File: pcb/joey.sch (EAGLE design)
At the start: 61 parts, among them J1 AVR_SPI_PRG_6PTH, U1 ATMEGA168, U2 TMP102, X1 USB-MICROB, Y1 13.56M

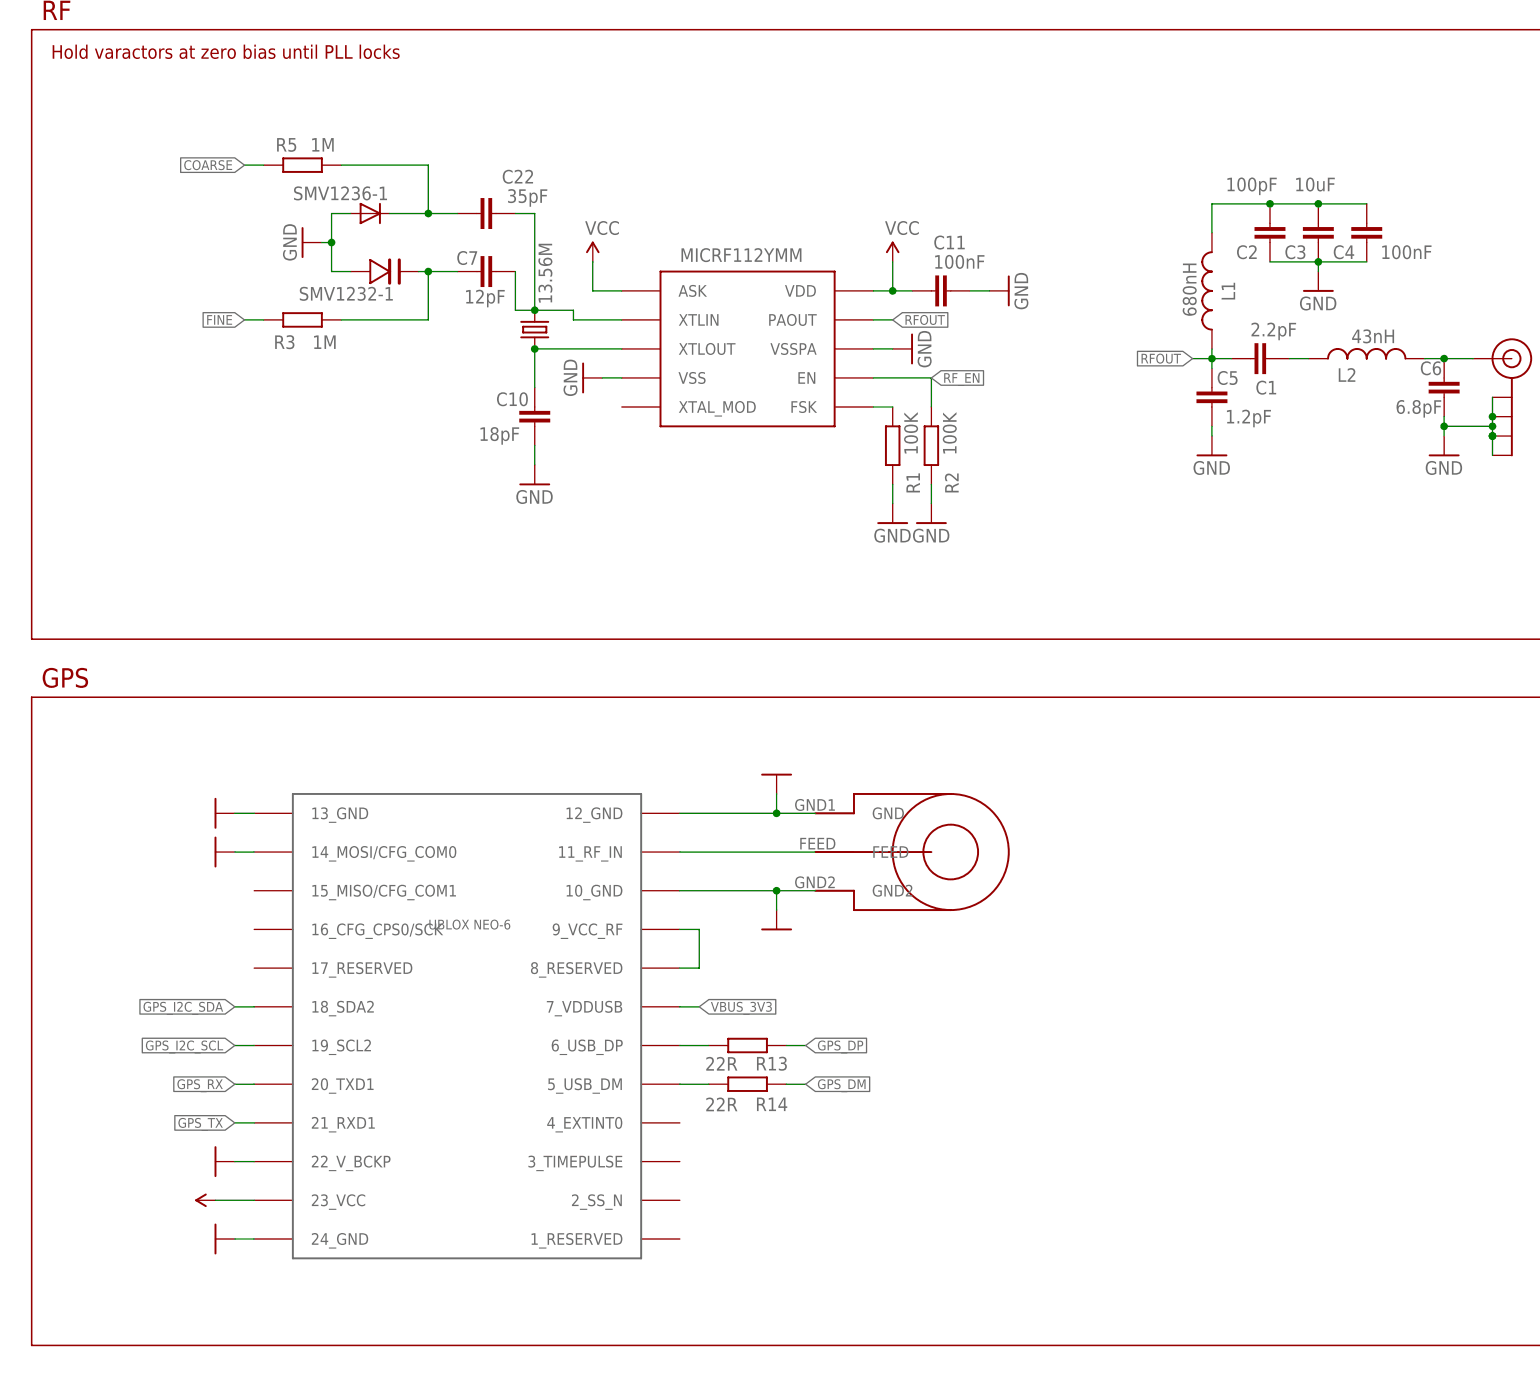
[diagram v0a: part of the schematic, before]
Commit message: Fixed filter bug in the schematic, almost finished routing
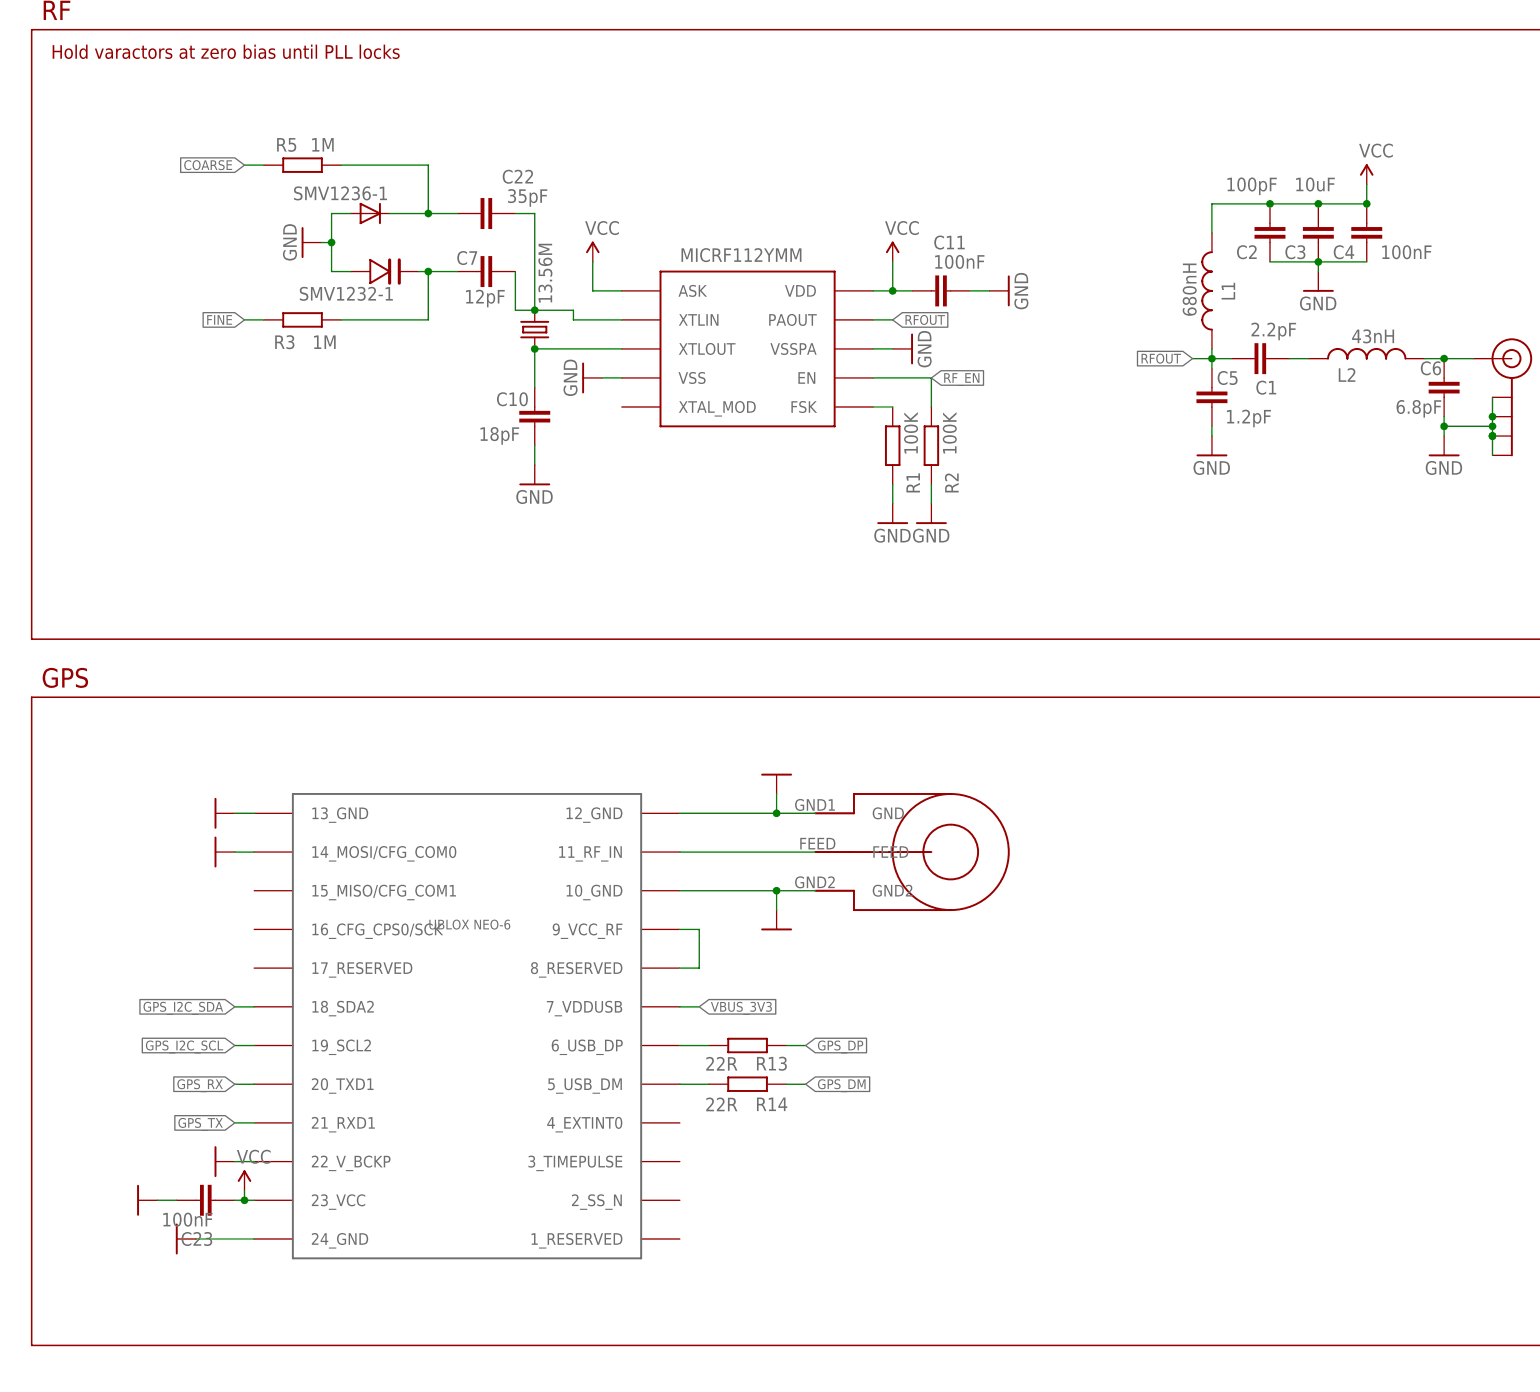
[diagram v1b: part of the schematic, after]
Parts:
- added C23: 100nF, rcl:C-EUC0603
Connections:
- removed net N$4: C2.2, C3.2, C4.2, L1.2
- new net COARSE_V: C22.1, R5.2, SMV1236-1.C
- net COARSE: no longer C22.1, R5.2, SMV1236-1.C
- net GND: now also C23.1
- net VCC: now also C2.2, C23.2, C3.2, C4.2, L1.2
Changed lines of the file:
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@@
 <part name="GND17" library="SparkFun" deviceset="GND" device=""/>
 <part name="GND18" library="SparkFun" deviceset="GND" device=""/>
-<part name="P+3" library="SparkFun" deviceset="VCC" device=""/>
 <part name="GND19" library="SparkFun" deviceset="GND" device=""/>
 <part name="GND20" library="SparkFun" deviceset="GND" device=""/>
@@
 <part name="GND34" library="SparkFun" deviceset="GND" device=""/>
 <part name="P+6" library="SparkFun" deviceset="VCC" device=""/>
+<part name="C23" library="rcl" deviceset="C-EU" device="C0603" value="100nF"/>
+<part name="GND35" library="SparkFun" deviceset="GND" device=""/>
+<part name="P+3" library="SparkFun" deviceset="VCC" device=""/>
+<part name="P+13" library="SparkFun" deviceset="VCC" device=""/>
 </parts>
 <sheets>
@@
 <instance part="U$2" gate="G$1" x="142.24" y="-62.23" smashed="yes" rot="R180"/>
 <instance part="U$3" gate="G$1" x="83.82" y="-67.31"/>
-<instance part="GND16" gate="1" x="48.26" y="-115.57" smashed="yes" rot="R270"/>
+<instance part="GND16" gate="1" x="43.18" y="-115.57" smashed="yes" rot="R270"/>
 <instance part="GND17" gate="1" x="48.26" y="-59.69" smashed="yes" rot="R270"/>
 <instance part="GND18" gate="1" x="48.26" y="-105.41" smashed="yes" rot="R270"/>
-<instance part="P+3" gate="1" x="48.26" y="-110.49" smashed="yes" rot="R90"/>
 <instance part="GND19" gate="1" x="121.92" y="-74.93" smashed="yes"/>
 <instance part="GND20" gate="1" x="121.92" y="-54.61" smashed="yes" rot="R180"/>
@@
 <instance part="GND34" gate="1" x="-123.19" y="-66.04" rot="R270"/>
 <instance part="P+6" gate="1" x="-95.25" y="-60.96" smashed="yes"/>
+<instance part="C23" gate="G$1" x="45.72" y="-110.49" smashed="yes" rot="R90">
+<attribute name="NAME" x="48.006" y="-114.681" size="1.778" layer="95" rot="R180"/>
+<attribute name="VALUE" x="48.006" y="-112.141" size="1.778" layer="96" rot="R180"/>
+</instance>
+<instance part="GND35" gate="1" x="38.1" y="-110.49" smashed="yes" rot="R270"/>
+<instance part="P+3" gate="1" x="52.07" y="-109.22"/>
+<instance part="P+13" gate="1" x="199.39" y="22.86"/>
 </instances>
 <busses>
@@
 <pinref part="U$3" gate="G$1" pin="24_GND"/>
 <pinref part="GND16" gate="1" pin="GND"/>
-<wire x1="53.34" y1="-115.57" x2="50.8" y2="-115.57" width="0.1524" layer="91"/>
+<wire x1="53.34" y1="-115.57" x2="45.72" y2="-115.57" width="0.1524" layer="91"/>
 </segment>
 <segment>
@@
 <wire x1="-113.03" y1="-66.04" x2="-120.65" y2="-66.04" width="0.1524" layer="91"/>
 </segment>
+<segment>
+<pinref part="C23" gate="G$1" pin="1"/>
+<wire x1="43.18" y1="-110.49" x2="40.64" y2="-110.49" width="0.1524" layer="91"/>
+<pinref part="GND35" gate="1" pin="GND"/>
+</segment>
 </net>
 <net name="VCC" class="0">
@@
 <pinref part="P+4" gate="1" pin="VCC"/>
 <pinref part="J1" gate="G$1" pin="2"/>
-</segment>
-<segment>
-<pinref part="P+3" gate="1" pin="VCC"/>
-<pinref part="U$3" gate="G$1" pin="23_VCC"/>
-<wire x1="48.26" y1="-110.49" x2="53.34" y2="-110.49" width="0.1524" layer="91"/>
 </segment>
 <segment>
@@
 <pinref part="P+6" gate="1" pin="VCC"/>
 </segment>
-</net>
-<net name="N$1" class="0">
-<segment>
-<wire x1="134.62" y1="-6.35" x2="137.16" y2="-6.35" width="0.1524" layer="91"/>
-<pinref part="U$1" gate="G$1" pin="FSK"/>
-<pinref part="R1" gate="G$1" pin="2"/>
-</segment>
-</net>
-<net name="RF_EN" class="0">
-<segment>
-<wire x1="134.62" y1="-2.54" x2="142.24" y2="-2.54" width="0.1524" layer="91"/>
-<wire x1="142.24" y1="-2.54" x2="142.24" y2="-6.35" width="0.1524" layer="91"/>
-<label x="142.24" y="-2.54" size="1.27" layer="95" xref="yes"/>
-<pinref part="U$1" gate="G$1" pin="EN"/>
-<pinref part="R2" gate="G$1" pin="2"/>
-</segment>
-<segment>
-<pinref part="U1" gate="G$1" pin="PC2(ADC2)"/>
-<wire x1="-44.45" y1="-60.96" x2="-41.91" y2="-60.96" width="0.1524" layer="91"/>
-<label x="-41.91" y="-60.96" size="1.27" layer="95" xref="yes"/>
-</segment>
-</net>
-<net name="RFOUT" class="0">
-<segment>
-<wire x1="179.07" y1="-1.27" x2="179.07" y2="0" width="0.1524" layer="91"/>
-<wire x1="179.07" y1="0" x2="179.07" y2="1.27" width="0.1524" layer="91"/>
-<wire x1="179.07" y1="0" x2="181.61" y2="0" width="0.1524" layer="91"/>
-<wire x1="179.07" y1="0" x2="176.53" y2="0" width="0.1524" layer="91"/>
-<junction x="179.07" y="0"/>
-<label x="176.53" y="0" size="1.27" layer="95" rot="R180" xref="yes"/>
-<pinref part="L1" gate="G$1" pin="1"/>
-<pinref part="C5" gate="G$1" pin="2"/>
-<pinref part="C1" gate="G$1" pin="1"/>
-</segment>
-<segment>
-<wire x1="134.62" y1="5.08" x2="137.16" y2="5.08" width="0.1524" layer="91"/>
-<label x="137.16" y="5.08" size="1.27" layer="95" xref="yes"/>
-<pinref part="U$1" gate="G$1" pin="PAOUT"/>
-</segment>
-</net>
-<net name="N$4" class="0">
+<segment>
+<pinref part="C23" gate="G$1" pin="2"/>
+<pinref part="U$3" gate="G$1" pin="23_VCC"/>
+<wire x1="50.8" y1="-110.49" x2="52.07" y2="-110.49" width="0.1524" layer="91"/>
+<pinref part="P+3" gate="1" pin="VCC"/>
+<wire x1="52.07" y1="-110.49" x2="53.34" y2="-110.49" width="0.1524" layer="91"/>
+<wire x1="52.07" y1="-109.22" x2="52.07" y2="-110.49" width="0.1524" layer="91"/>
+<junction x="52.07" y="-110.49"/>
+</segment>
 <segment>
 <wire x1="179.07" y1="16.51" x2="179.07" y2="20.32" width="0.1524" layer="91"/>
@@
 <pinref part="C3" gate="G$1" pin="2"/>
 <pinref part="C4" gate="G$1" pin="2"/>
+<pinref part="P+13" gate="1" pin="VCC"/>
+<wire x1="199.39" y1="22.86" x2="199.39" y2="20.32" width="0.1524" layer="91"/>
+<junction x="199.39" y="20.32"/>
+</segment>
+</net>
+<net name="N$1" class="0">
+<segment>
+<wire x1="134.62" y1="-6.35" x2="137.16" y2="-6.35" width="0.1524" layer="91"/>
+<pinref part="U$1" gate="G$1" pin="FSK"/>
+<pinref part="R1" gate="G$1" pin="2"/>
+</segment>
+</net>
+<net name="RF_EN" class="0">
+<segment>
+<wire x1="134.62" y1="-2.54" x2="142.24" y2="-2.54" width="0.1524" layer="91"/>
+<wire x1="142.24" y1="-2.54" x2="142.24" y2="-6.35" width="0.1524" layer="91"/>
+<label x="142.24" y="-2.54" size="1.27" layer="95" xref="yes"/>
+<pinref part="U$1" gate="G$1" pin="EN"/>
+<pinref part="R2" gate="G$1" pin="2"/>
+</segment>
+<segment>
+<pinref part="U1" gate="G$1" pin="PC2(ADC2)"/>
+<wire x1="-44.45" y1="-60.96" x2="-41.91" y2="-60.96" width="0.1524" layer="91"/>
+<label x="-41.91" y="-60.96" size="1.27" layer="95" xref="yes"/>
+</segment>
+</net>
+<net name="RFOUT" class="0">
+<segment>
+<wire x1="179.07" y1="-1.27" x2="179.07" y2="0" width="0.1524" layer="91"/>
+<wire x1="179.07" y1="0" x2="179.07" y2="1.27" width="0.1524" layer="91"/>
+<wire x1="179.07" y1="0" x2="181.61" y2="0" width="0.1524" layer="91"/>
+<wire x1="179.07" y1="0" x2="176.53" y2="0" width="0.1524" layer="91"/>
+<junction x="179.07" y="0"/>
+<label x="176.53" y="0" size="1.27" layer="95" rot="R180" xref="yes"/>
+<pinref part="L1" gate="G$1" pin="1"/>
+<pinref part="C5" gate="G$1" pin="2"/>
+<pinref part="C1" gate="G$1" pin="1"/>
+</segment>
+<segment>
+<wire x1="134.62" y1="5.08" x2="137.16" y2="5.08" width="0.1524" layer="91"/>
+<label x="137.16" y="5.08" size="1.27" layer="95" xref="yes"/>
+<pinref part="U$1" gate="G$1" pin="PAOUT"/>
 </segment>
 </net>
@@
 <net name="COARSE" class="0">
 <segment>
-<wire x1="76.2" y1="19.05" x2="80.01" y2="19.05" width="0.1524" layer="91"/>
-<wire x1="76.2" y1="19.05" x2="76.2" y2="25.4" width="0.1524" layer="91"/>
-<wire x1="76.2" y1="25.4" x2="64.77" y2="25.4" width="0.1524" layer="91"/>
-<wire x1="71.12" y1="19.05" x2="76.2" y2="19.05" width="0.1524" layer="91"/>
-<junction x="76.2" y="19.05"/>
-<pinref part="C22" gate="G$1" pin="1"/>
-<pinref part="R5" gate="G$1" pin="2"/>
-<pinref part="SMV1236-1" gate="G$1" pin="C"/>
-</segment>
-<segment>
 <wire x1="54.61" y1="25.4" x2="52.07" y2="25.4" width="0.1524" layer="91"/>
 <label x="52.07" y="25.4" size="1.27" layer="95" rot="R180" xref="yes"/>
@@
 </segment>
 </net>
+<net name="COARSE_V" class="0">
+<segment>
+<wire x1="76.2" y1="19.05" x2="80.01" y2="19.05" width="0.1524" layer="91"/>
+<wire x1="76.2" y1="19.05" x2="76.2" y2="25.4" width="0.1524" layer="91"/>
+<wire x1="76.2" y1="25.4" x2="64.77" y2="25.4" width="0.1524" layer="91"/>
+<wire x1="71.12" y1="19.05" x2="76.2" y2="19.05" width="0.1524" layer="91"/>
+<junction x="76.2" y="19.05"/>
+<pinref part="C22" gate="G$1" pin="1"/>
+<pinref part="R5" gate="G$1" pin="2"/>
+<pinref part="SMV1236-1" gate="G$1" pin="C"/>
+</segment>
+</net>

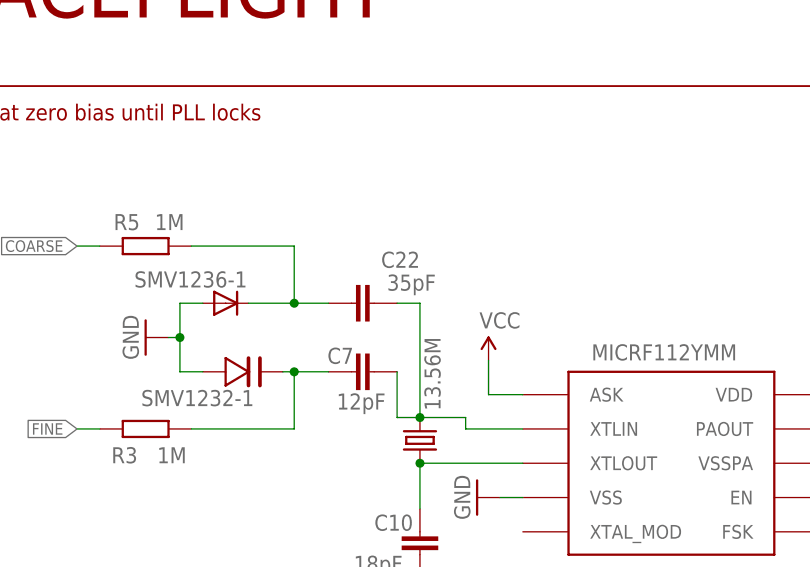
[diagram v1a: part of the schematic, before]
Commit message: Finished routing, updated completed BOM for v1.0
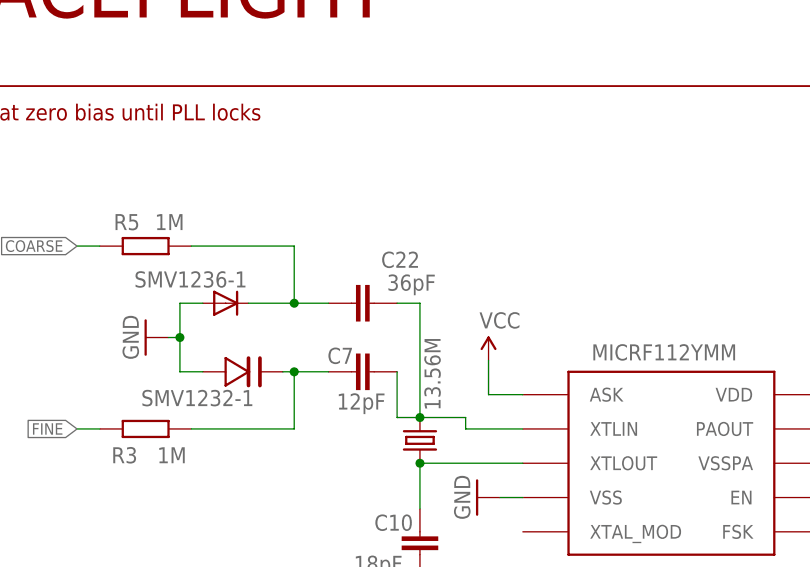
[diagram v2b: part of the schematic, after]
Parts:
- C22: value 35pF -> 36pF
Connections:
- removed net N$16: USB_ESD.VBUS, X1.VBUS
- net VBUS: now also USB_ESD.VBUS, X1.VBUS
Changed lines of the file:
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@@
 <part name="C18" library="rcl" deviceset="C-EU" device="C0603" value="18pF"/>
 <part name="GND15" library="SparkFun" deviceset="GND" device=""/>
-<part name="C22" library="rcl" deviceset="C-EU" device="C0603" value="35pF"/>
+<part name="C22" library="rcl" deviceset="C-EU" device="C0603" value="36pF"/>
 <part name="R5" library="rcl" deviceset="R-EU_" device="R0603" value="1M"/>
 <part name="SMV1236-1" library="SparkFun" deviceset="DIODE" device="SOD"/>
@@
 <label x="-120.65" y="-27.94" size="1.27" layer="95" rot="R180" xref="yes"/>
 </segment>
-</net>
-<net name="N$16" class="0">
 <segment>
 <pinref part="X1" gate="G$1" pin="VBUS"/>
